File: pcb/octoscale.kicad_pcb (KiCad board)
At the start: 2 copper layers, 60 x 96.5 mm, 115 parts, among them J1 USB_C_Receptacle_USB2.0 TYPE-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, J2 Conn_01x04_Male, J3 Molex picoblade vertical C122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, J4 JST-SH, stemma, J5 JST-SH, J6 JST-SH, J7 Conn_01x04_Male, Q1 AO3415_C181094, Q2 MMBT44032T, Q3 S8050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

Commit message: basic schematic and pcb changes
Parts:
- removed JP2: SolderJumper_2_Bridged, Jumper:SolderJumper-2_P1.3mm_Bridged_RoundedPad1.0x1.5mm
- removed R15: 10K, Resistor_SMD:R_0805_2012Metric_Pad1.20x1.40mm_HandSolder
- removed the REF** at (154.0, 134.7)
- added D17: PMEG2010AEB, Diode_SMD:D_SOD-523, B.Cu at (165.9, 58.4)
- R3: value 100k -> 1.5k
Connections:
- C10 pad 1: +3V3 -> +3.3V
- C12 pad 1: +3V3 -> +3.3V
- C13 pad 1: +3V3 -> +3.3V
- C14 pad 1: +3V3 -> +3.3V
- C19 pad 1: +BATT -> +3.3V
- C2 pad 1: +3V3 -> +3.3V
- C20 pad 1: +BATT -> +3.3V
- C21 pad 1: +BATT -> +3.3V
- C22 pad 1: +BATT -> +3.3V
- C23 pad 1: +BATT -> +3.3V
- C24 pad 1: +BATT -> +3.3V
- C25 pad 1: +BATT -> +3.3V
- C26 pad 1: +BATT -> +3.3V
- C27 pad 1: +BATT -> +3.3V
- C28 pad 2: +3V3 -> +3.3V
- C29 pad 1: +3V3 -> +3.3V
- C8 pad 1: +3V3 -> +3.3V
- C9 pad 1: +3V3 -> +3.3V
- D1 pad 2: +BATT -> +3.3V
- D10 pad 2: +BATT -> +3.3V
- D11 pad 2: +BATT -> +3.3V
- D12 pad 2: +BATT -> +3.3V
- D14 pad 2: +3V3 -> +3.3V
- D15 pad 1: +3V3 -> +3.3V
- D3 pad 2: +BATT -> +3.3V
- D6 pad 2: +BATT -> +3.3V
- D7 pad 2: +BATT -> +3.3V
- D8 pad 2: +BATT -> +3.3V
- D9 pad 2: +BATT -> +3.3V
- DS1 pad 11: +3V3 -> +3.3V
- DS1 pad 13: +3V3 -> +3.3V
- DS1 pad 6: +3V3 -> +3.3V
- DS1 pad 9: +3V3 -> +3.3V
- J4 pad 2: +3V3 -> +3.3V
- J5 pad 2: +3V3 -> +3.3V
- J6 pad 2: +3V3 -> +3.3V
- LS1 pad 1: +3V3 -> +3.3V
- Q2 pad 2: +3V3 -> +3.3V
- R10 pad 1: +3V3 -> +3.3V
- R18 pad 1: +3V3 -> +3.3V
- R19 pad 1: +3V3 -> +3.3V
- TP12 pad 1: +3V3 -> +3.3V
- U2 pad 1: +3V3 -> +3.3V
- U4 pad 1: +3V3 -> +3.3V
- U4 pad 16: +3V3 -> +3.3V
- U5 pad 2: +3V3 -> +3.3V
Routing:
- net +3.3V: track 0.00 -> 444.2 mm, vias 0 -> 12
- net +BATT: track 316.1 -> 30.8 mm, vias 6 -> 0
- net +3V3: track 248.5 -> 0.00 mm, vias 8 -> 0
- net VBUS: track 53.7 -> 55.1 mm
- net LDO_EN: track 53.2 -> 52.4 mm
- added copper zone on B.Cu, net +3.3V
- removed copper zone on B.Cu, net +3V3
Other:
- board text removed: "cut to disable wake on usb"

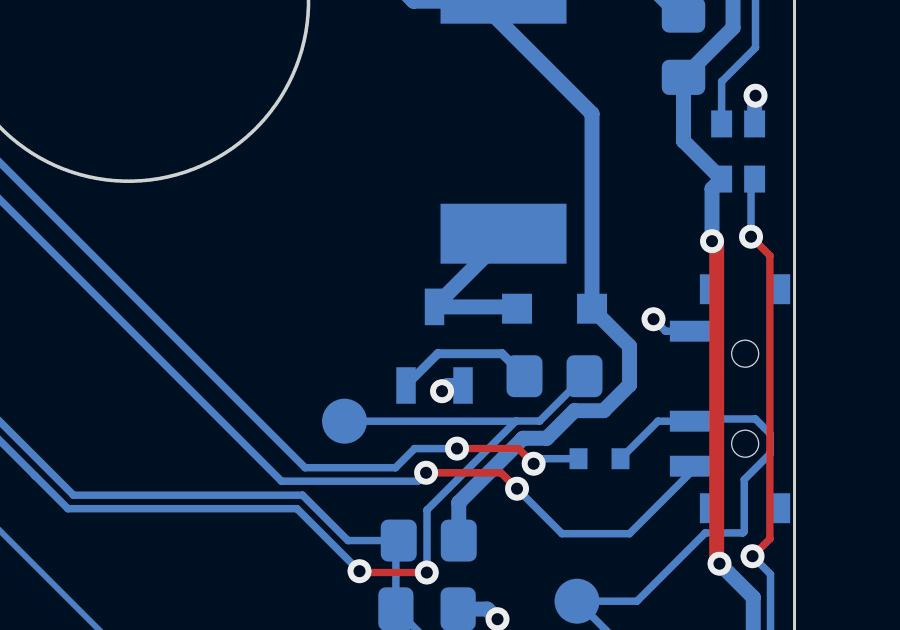
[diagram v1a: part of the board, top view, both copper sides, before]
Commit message: fix speaker transistor
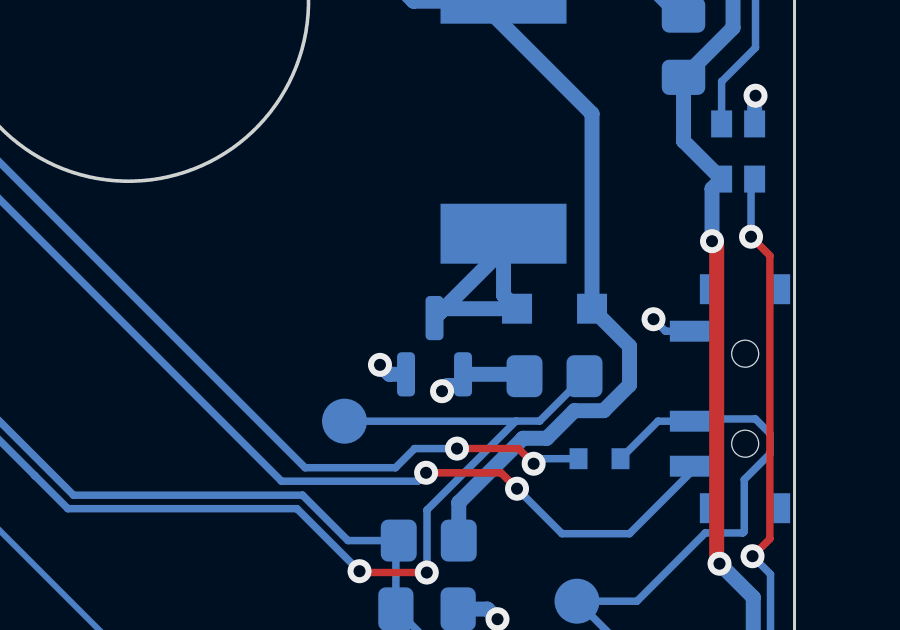
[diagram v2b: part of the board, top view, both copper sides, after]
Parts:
- Q3: value S8050 -> SS8050; footprint Package_TO_SOT_SMD:TSOT-23 -> Package_TO_SOT_SMD:SOT-23
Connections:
- Q3 pad 1: GND -> Net-(Q3-Pad1)
- Q3 pad 2: Net-(Q3-Pad2) -> GND
- R14 pad 2: Net-(Q3-Pad2) -> Net-(Q3-Pad1)
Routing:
- net Net-(Q3-Pad2): track 4.70 -> 0.00 mm
- net Net-(D15-Pad2): track 6.17 -> 9.57 mm
- net Net-(Q3-Pad1): track 0.00 -> 2.85 mm, vias 0 -> 1

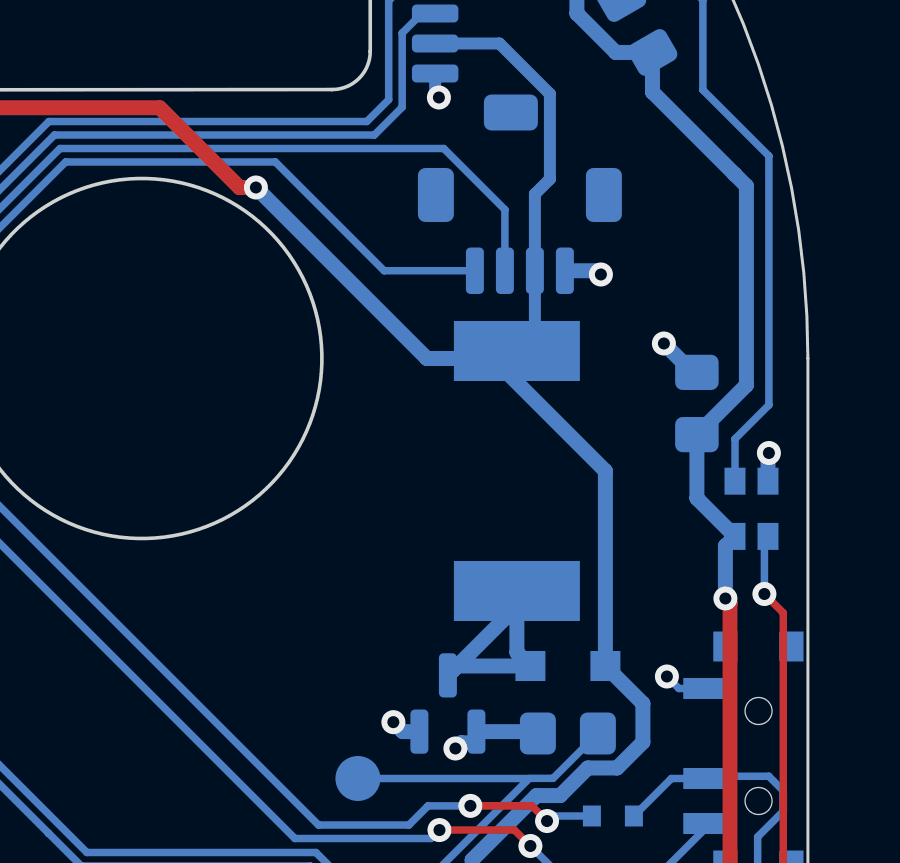
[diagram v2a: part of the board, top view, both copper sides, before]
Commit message: Fix buzzer footprint
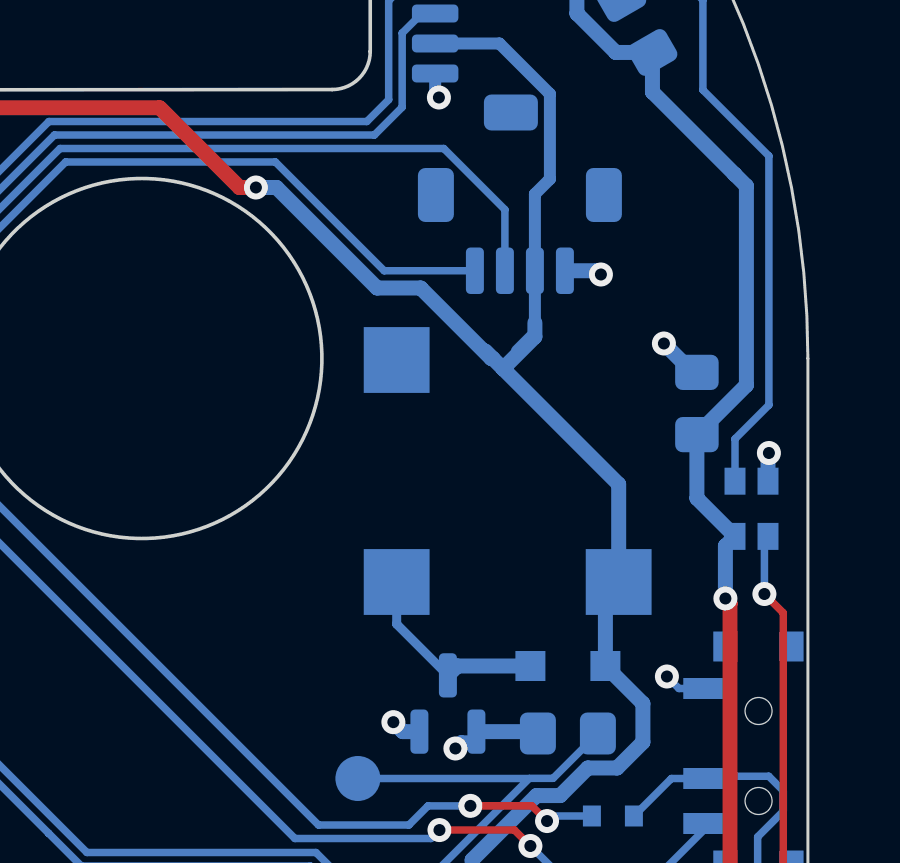
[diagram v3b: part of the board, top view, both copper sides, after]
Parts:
- LS1: footprint Buzzer_Beeper:Buzzer_CUI_CPT-9019S-SMT -> Buzzer_Beeper:MagneticBuzzer_Kobitone_254-EMB84Q-RO
- moved LS1 0.31 mm to (190.0, 78.8), turned to 90 degrees
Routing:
- net Net-(D15-Pad2): track 9.57 -> 6.88 mm
- net +3.3V: track 444.2 -> 446.6 mm

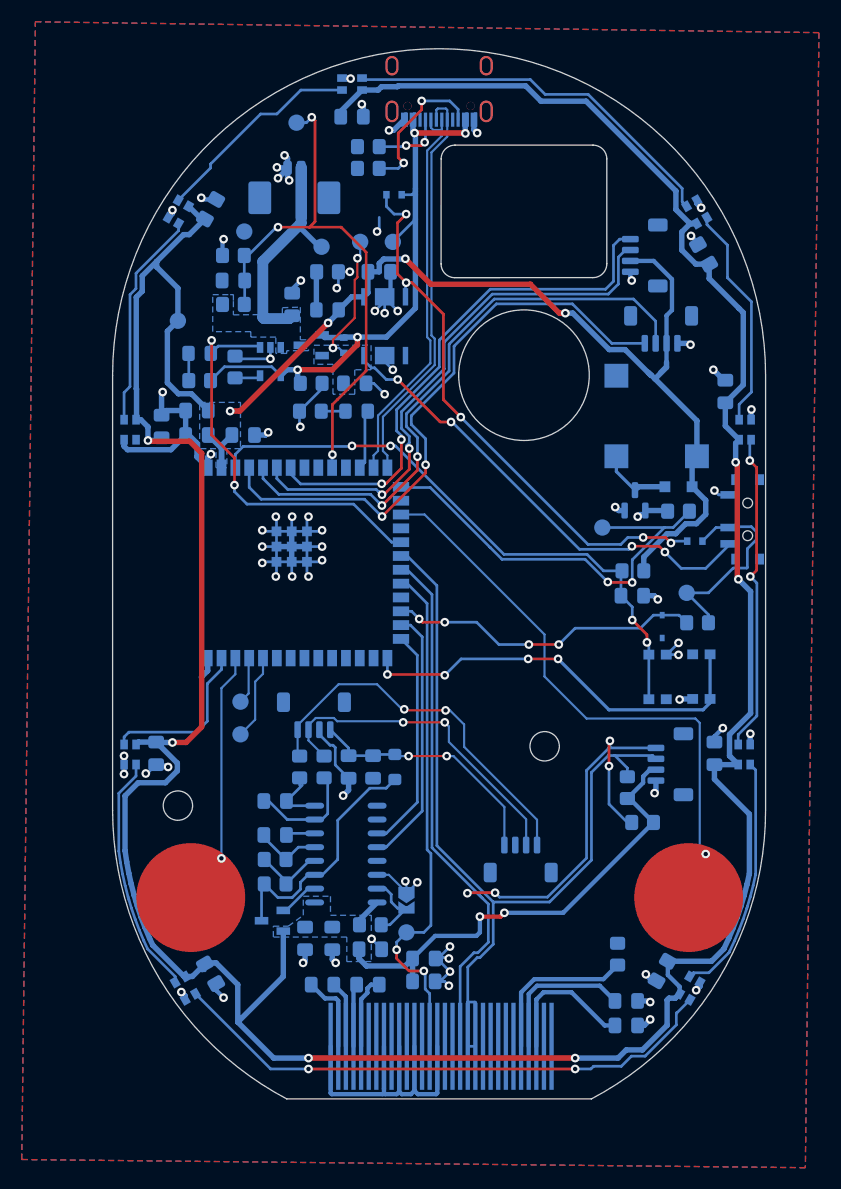
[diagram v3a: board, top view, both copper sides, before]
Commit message: Fix drc errors
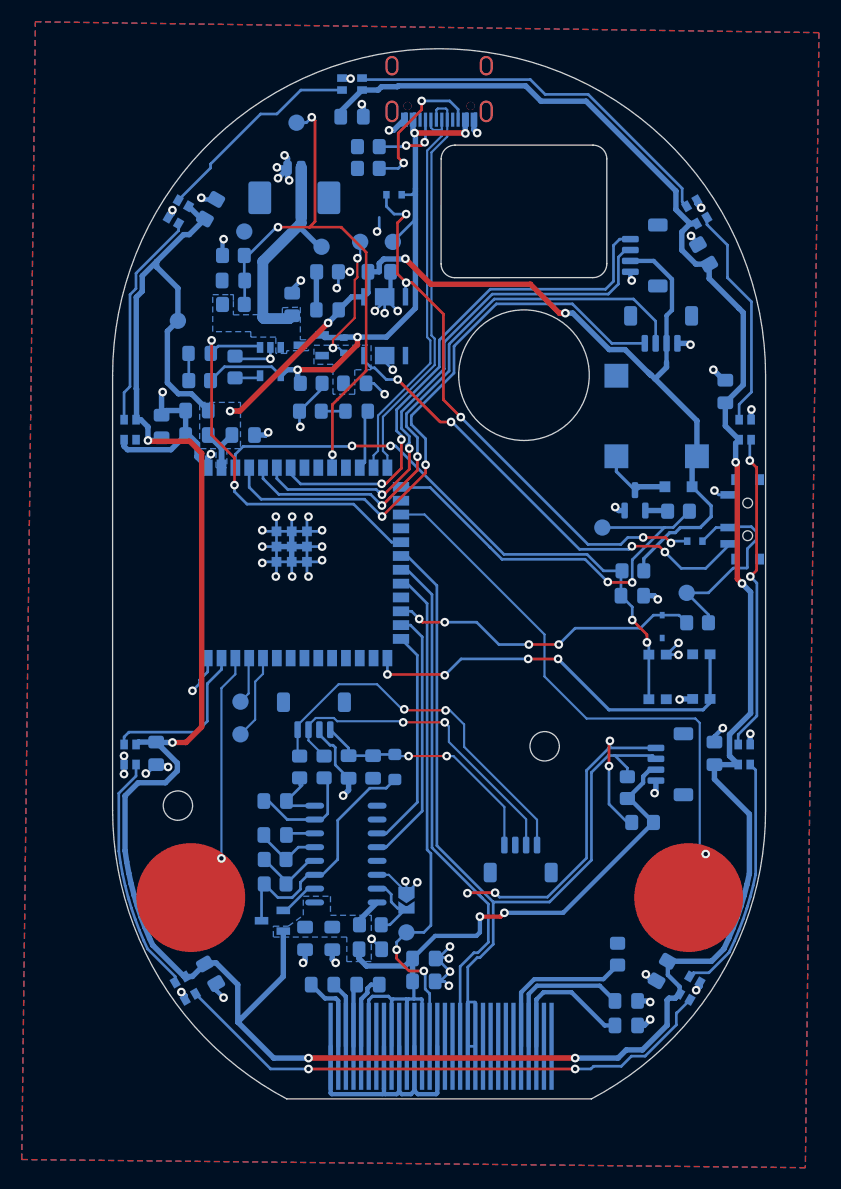
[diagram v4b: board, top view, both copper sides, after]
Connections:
- R12 pad 1: +3V3 -> +3.3V
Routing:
- net +3.3V: track 446.6 -> 477.5 mm
- net GND: track 186.6 -> 188.2 mm, vias 72 -> 73
- net Net-(Q3-Pad1): track 2.85 -> 2.08 mm, vias 1 -> 0
